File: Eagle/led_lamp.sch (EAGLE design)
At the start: 11 parts

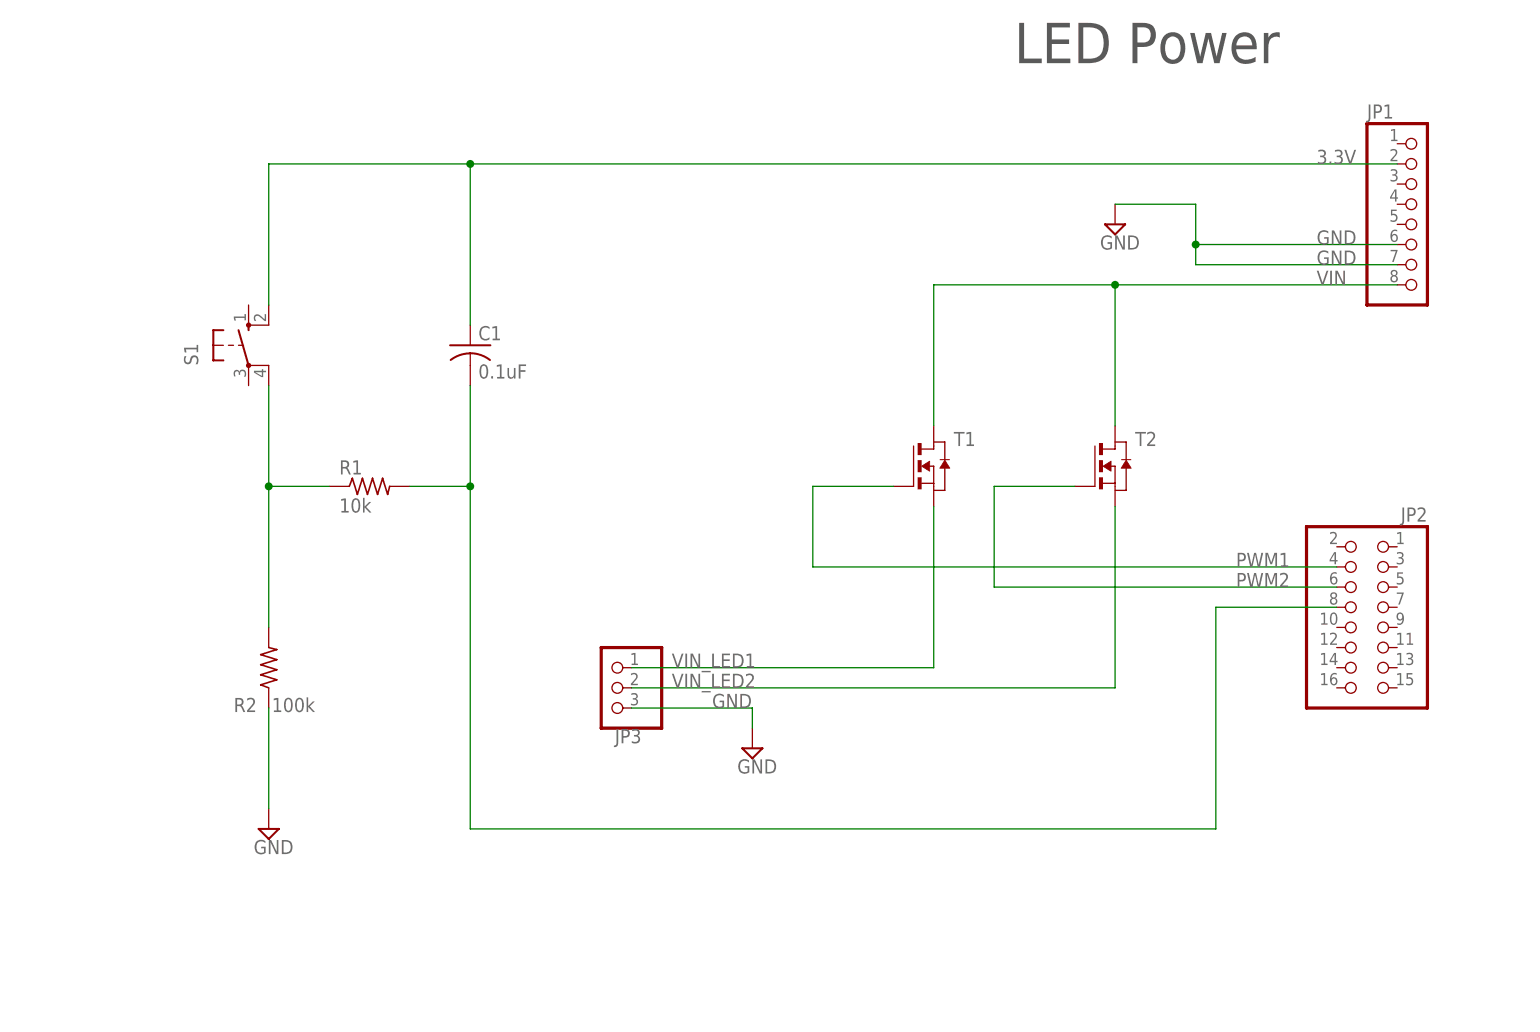
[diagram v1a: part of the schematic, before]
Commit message: Added pwr button to eagle pcb
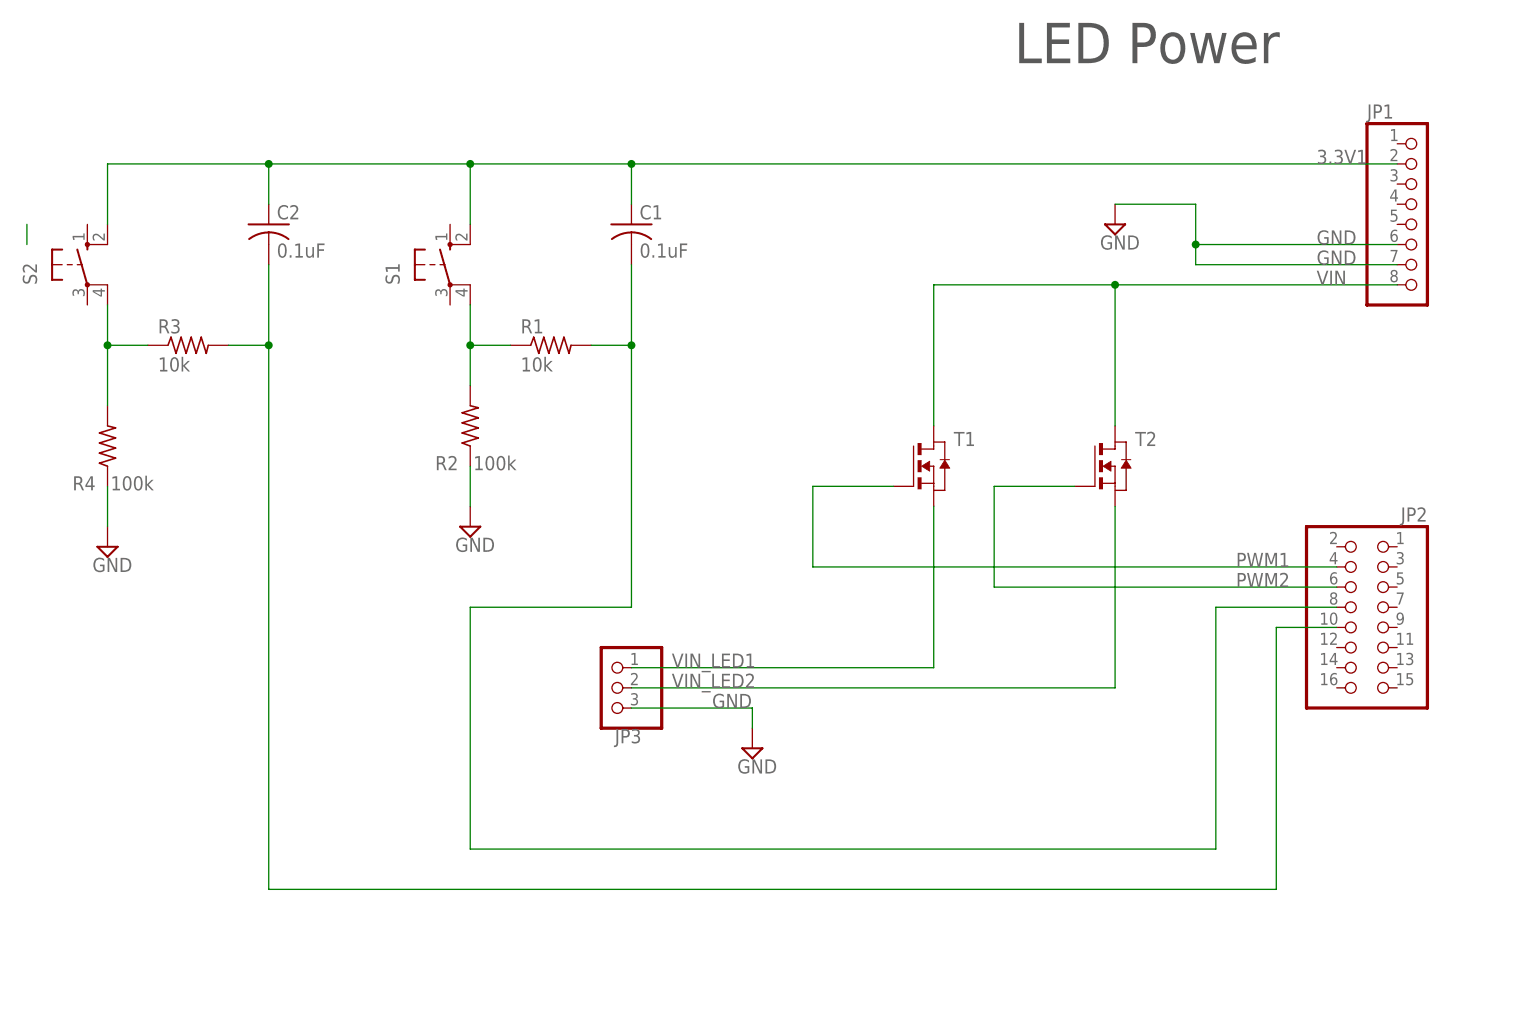
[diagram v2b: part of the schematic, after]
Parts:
- added C2: 0.1uF, rcl:C-USC1206K
- added R3: 10k, rcl:R-US_R1206
- added R4: 100k, rcl:R-US_R1206
- added S2: (no value), switch-omron:10-XX
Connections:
- removed net 3.3V: C1.1, JP1.2, S1.S1
- new net 3.3V1: C1.1, C2.1, JP1.2, S1.S1, S2.S1
- new net N$3: R3.1, R4.2, S2.P1
- new net N$4: C2.2, JP2.10, R3.2
- net GND: now also R4.1
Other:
- moved on the sheet: C1, R1, R2, S1
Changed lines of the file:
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@@
 <part name="C1" library="rcl" library_urn="urn:adsk.eagle:library:334" deviceset="C-US" device="C1206K" package3d_urn="urn:adsk.eagle:package:23682/2" value="0.1uF"/>
 <part name="SUPPLY4" library="supply2" library_urn="urn:adsk.eagle:library:372" deviceset="GND" device=""/>
+<part name="S2" library="switch-omron" library_urn="urn:adsk.eagle:library:377" deviceset="10-XX" device="" package3d_urn="urn:adsk.eagle:package:27496/1"/>
+<part name="R3" library="rcl" library_urn="urn:adsk.eagle:library:334" deviceset="R-US_" device="R1206" package3d_urn="urn:adsk.eagle:package:23540/2" value="10k"/>
+<part name="R4" library="rcl" library_urn="urn:adsk.eagle:library:334" deviceset="R-US_" device="R1206" package3d_urn="urn:adsk.eagle:package:23540/2" value="100k"/>
+<part name="C2" library="rcl" library_urn="urn:adsk.eagle:library:334" deviceset="C-US" device="C1206K" package3d_urn="urn:adsk.eagle:package:23682/2" value="0.1uF"/>
+<part name="SUPPLY5" library="supply2" library_urn="urn:adsk.eagle:library:372" deviceset="GND" device=""/>
 </parts>
 <sheets>
@@
 <attribute name="VALUE" x="142.875" y="172.085" size="1.778" layer="96"/>
 </instance>
-<instance part="S1" gate="1" x="35.56" y="160.02" smashed="yes">
-<attribute name="NAME" x="29.21" y="157.48" size="1.778" layer="95" rot="R90"/>
-<attribute name="VALUE" x="31.75" y="163.195" size="1.778" layer="96" rot="R90"/>
-</instance>
-<instance part="R1" gate="G$1" x="50.8" y="142.24" smashed="yes">
-<attribute name="NAME" x="46.99" y="143.7386" size="1.778" layer="95"/>
-<attribute name="VALUE" x="46.99" y="138.938" size="1.778" layer="96"/>
-</instance>
-<instance part="R2" gate="G$1" x="38.1" y="119.38" smashed="yes" rot="R90">
-<attribute name="NAME" x="36.6014" y="115.57" size="1.778" layer="95" rot="R180"/>
-<attribute name="VALUE" x="43.942" y="115.57" size="1.778" layer="96" rot="R180"/>
-</instance>
-<instance part="C1" gate="G$1" x="63.5" y="160.02" smashed="yes">
-<attribute name="NAME" x="64.516" y="160.655" size="1.778" layer="95"/>
-<attribute name="VALUE" x="64.516" y="155.829" size="1.778" layer="96"/>
-</instance>
-<instance part="SUPPLY4" gate="GND" x="38.1" y="99.06" smashed="yes">
-<attribute name="VALUE" x="36.195" y="95.885" size="1.778" layer="96"/>
+<instance part="S1" gate="1" x="60.96" y="170.18" smashed="yes">
+<attribute name="NAME" x="54.61" y="167.64" size="1.778" layer="95" rot="R90"/>
+<attribute name="VALUE" x="57.15" y="173.355" size="1.778" layer="96" rot="R90"/>
+</instance>
+<instance part="R1" gate="G$1" x="73.66" y="160.02" smashed="yes">
+<attribute name="NAME" x="69.85" y="161.5186" size="1.778" layer="95"/>
+<attribute name="VALUE" x="69.85" y="156.718" size="1.778" layer="96"/>
+</instance>
+<instance part="R2" gate="G$1" x="63.5" y="149.86" smashed="yes" rot="R90">
+<attribute name="NAME" x="62.0014" y="146.05" size="1.778" layer="95" rot="R180"/>
+<attribute name="VALUE" x="69.342" y="146.05" size="1.778" layer="96" rot="R180"/>
+</instance>
+<instance part="C1" gate="G$1" x="83.82" y="175.26" smashed="yes">
+<attribute name="NAME" x="84.836" y="175.895" size="1.778" layer="95"/>
+<attribute name="VALUE" x="84.836" y="171.069" size="1.778" layer="96"/>
+</instance>
+<instance part="SUPPLY4" gate="GND" x="63.5" y="137.16" smashed="yes">
+<attribute name="VALUE" x="61.595" y="133.985" size="1.778" layer="96"/>
+</instance>
+<instance part="S2" gate="1" x="15.24" y="170.18" smashed="yes">
+<attribute name="NAME" x="8.89" y="167.64" size="1.778" layer="95" rot="R90"/>
+<attribute name="VALUE" x="11.43" y="173.355" size="1.778" layer="96" rot="R90"/>
+</instance>
+<instance part="R3" gate="G$1" x="27.94" y="160.02" smashed="yes">
+<attribute name="NAME" x="24.13" y="161.5186" size="1.778" layer="95"/>
+<attribute name="VALUE" x="24.13" y="156.718" size="1.778" layer="96"/>
+</instance>
+<instance part="R4" gate="G$1" x="17.78" y="147.32" smashed="yes" rot="R90">
+<attribute name="NAME" x="16.2814" y="143.51" size="1.778" layer="95" rot="R180"/>
+<attribute name="VALUE" x="23.622" y="143.51" size="1.778" layer="96" rot="R180"/>
+</instance>
+<instance part="C2" gate="G$1" x="38.1" y="175.26" smashed="yes">
+<attribute name="NAME" x="39.116" y="175.895" size="1.778" layer="95"/>
+<attribute name="VALUE" x="39.116" y="171.069" size="1.778" layer="96"/>
+</instance>
+<instance part="SUPPLY5" gate="GND" x="17.78" y="134.62" smashed="yes">
+<attribute name="VALUE" x="15.875" y="131.445" size="1.778" layer="96"/>
 </instance>
 </instances>
@@
 <pinref part="R2" gate="G$1" pin="1"/>
 <pinref part="SUPPLY4" gate="GND" pin="GND"/>
-<wire x1="38.1" y1="114.3" x2="38.1" y2="101.6" width="0.1524" layer="91"/>
+<wire x1="63.5" y1="144.78" x2="63.5" y2="139.7" width="0.1524" layer="91"/>
+</segment>
+<segment>
+<pinref part="R4" gate="G$1" pin="1"/>
+<pinref part="SUPPLY5" gate="GND" pin="GND"/>
+<wire x1="17.78" y1="142.24" x2="17.78" y2="137.16" width="0.1524" layer="91"/>
 </segment>
 </net>
@@
 <segment>
 <pinref part="S1" gate="1" pin="P1"/>
-<wire x1="38.1" y1="154.94" x2="38.1" y2="142.24" width="0.1524" layer="91"/>
+<wire x1="63.5" y1="165.1" x2="63.5" y2="160.02" width="0.1524" layer="91"/>
 <pinref part="R1" gate="G$1" pin="1"/>
-<wire x1="38.1" y1="142.24" x2="45.72" y2="142.24" width="0.1524" layer="91"/>
+<wire x1="63.5" y1="160.02" x2="68.58" y2="160.02" width="0.1524" layer="91"/>
 <pinref part="R2" gate="G$1" pin="2"/>
-<wire x1="38.1" y1="124.46" x2="38.1" y2="142.24" width="0.1524" layer="91"/>
-<junction x="38.1" y="142.24"/>
+<wire x1="63.5" y1="154.94" x2="63.5" y2="160.02" width="0.1524" layer="91"/>
+<junction x="63.5" y="160.02"/>
 </segment>
 </net>
@@
 <pinref part="R1" gate="G$1" pin="2"/>
 <pinref part="C1" gate="G$1" pin="2"/>
-<wire x1="55.88" y1="142.24" x2="63.5" y2="142.24" width="0.1524" layer="91"/>
-<wire x1="63.5" y1="142.24" x2="63.5" y2="154.94" width="0.1524" layer="91"/>
-<wire x1="63.5" y1="142.24" x2="63.5" y2="99.06" width="0.1524" layer="91"/>
-<junction x="63.5" y="142.24"/>
-<wire x1="63.5" y1="99.06" x2="157.48" y2="99.06" width="0.1524" layer="91"/>
+<wire x1="78.74" y1="160.02" x2="83.82" y2="160.02" width="0.1524" layer="91"/>
+<wire x1="83.82" y1="160.02" x2="83.82" y2="170.18" width="0.1524" layer="91"/>
+<wire x1="83.82" y1="160.02" x2="83.82" y2="127" width="0.1524" layer="91"/>
+<wire x1="83.82" y1="127" x2="63.5" y2="127" width="0.1524" layer="91"/>
+<wire x1="63.5" y1="127" x2="63.5" y2="96.52" width="0.1524" layer="91"/>
+<junction x="83.82" y="160.02"/>
+<wire x1="63.5" y1="96.52" x2="157.48" y2="96.52" width="0.1524" layer="91"/>
 <pinref part="JP2" gate="A" pin="8"/>
-<wire x1="157.48" y1="99.06" x2="157.48" y2="127" width="0.1524" layer="91"/>
+<wire x1="157.48" y1="96.52" x2="157.48" y2="127" width="0.1524" layer="91"/>
 <wire x1="157.48" y1="127" x2="172.72" y2="127" width="0.1524" layer="91"/>
 </segment>
 </net>
-<net name="3.3V" class="0">
-<segment>
+<net name="N$3" class="0">
+<segment>
+<pinref part="S2" gate="1" pin="P1"/>
+<wire x1="17.78" y1="165.1" x2="17.78" y2="160.02" width="0.1524" layer="91"/>
+<pinref part="R3" gate="G$1" pin="1"/>
+<wire x1="17.78" y1="160.02" x2="22.86" y2="160.02" width="0.1524" layer="91"/>
+<pinref part="R4" gate="G$1" pin="2"/>
+<wire x1="17.78" y1="152.4" x2="17.78" y2="160.02" width="0.1524" layer="91"/>
+<junction x="17.78" y="160.02"/>
+</segment>
+</net>
+<net name="N$4" class="0">
+<segment>
+<pinref part="R3" gate="G$1" pin="2"/>
+<pinref part="C2" gate="G$1" pin="2"/>
+<wire x1="33.02" y1="160.02" x2="38.1" y2="160.02" width="0.1524" layer="91"/>
+<wire x1="38.1" y1="160.02" x2="38.1" y2="170.18" width="0.1524" layer="91"/>
+<junction x="38.1" y="160.02"/>
+<wire x1="38.1" y1="160.02" x2="38.1" y2="91.44" width="0.1524" layer="91"/>
+<wire x1="38.1" y1="91.44" x2="165.1" y2="91.44" width="0.1524" layer="91"/>
+<wire x1="165.1" y1="91.44" x2="165.1" y2="124.46" width="0.1524" layer="91"/>
+<pinref part="JP2" gate="A" pin="10"/>
+<wire x1="165.1" y1="124.46" x2="172.72" y2="124.46" width="0.1524" layer="91"/>
+</segment>
+</net>
+<net name="3.3V1" class="0">
+<segment>
+<pinref part="S2" gate="1" pin="S1"/>
+<wire x1="17.78" y1="175.26" x2="17.78" y2="182.88" width="0.1524" layer="91"/>
+<wire x1="17.78" y1="182.88" x2="38.1" y2="182.88" width="0.1524" layer="91"/>
+<pinref part="C2" gate="G$1" pin="1"/>
+<wire x1="38.1" y1="182.88" x2="38.1" y2="177.8" width="0.1524" layer="91"/>
 <pinref part="S1" gate="1" pin="S1"/>
-<wire x1="38.1" y1="165.1" x2="38.1" y2="182.88" width="0.1524" layer="91"/>
+<wire x1="63.5" y1="175.26" x2="63.5" y2="182.88" width="0.1524" layer="91"/>
 <wire x1="38.1" y1="182.88" x2="63.5" y2="182.88" width="0.1524" layer="91"/>
+<junction x="38.1" y="182.88"/>
 <pinref part="C1" gate="G$1" pin="1"/>
-<wire x1="63.5" y1="182.88" x2="63.5" y2="162.56" width="0.1524" layer="91"/>
+<wire x1="83.82" y1="182.88" x2="83.82" y2="177.8" width="0.1524" layer="91"/>
 <pinref part="JP1" gate="A" pin="2"/>
-<wire x1="180.34" y1="182.88" x2="63.5" y2="182.88" width="0.1524" layer="91"/>
+<wire x1="180.34" y1="182.88" x2="83.82" y2="182.88" width="0.1524" layer="91"/>
+<label x="170.18" y="182.88" size="1.778" layer="95"/>
+<wire x1="63.5" y1="182.88" x2="83.82" y2="182.88" width="0.1524" layer="91"/>
 <junction x="63.5" y="182.88"/>
-<label x="170.18" y="182.88" size="1.778" layer="95"/>
-</segment>
-</net>
+<junction x="83.82" y="182.88"/>
+</segment>
+</net>
+<net name="N$5" class="0">
+<segment>
+<wire x1="7.62" y1="175.26" x2="7.62" y2="172.72" width="0.1524" layer="91"/>
+</segment>
+</net>
